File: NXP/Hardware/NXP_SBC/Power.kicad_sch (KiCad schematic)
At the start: 101 parts, among them J6 USB_C_Receptacle_PowerOnly_6P, J7 Screw_Terminal_01x02, Q1 DMN3150L-7, Q2 DMN3150L-7, Q3 DMN3150L-7, Q4 DMN3150L-7, Q5 DMN3150L-7, Q6 DMN3150L-7, Q8 DMN3150L-7, U11 AP3401, U3 AP3401, U4 AP3401, U5 MP2144GJ-P, U6 MAX811REUS-T, U9 AP3401

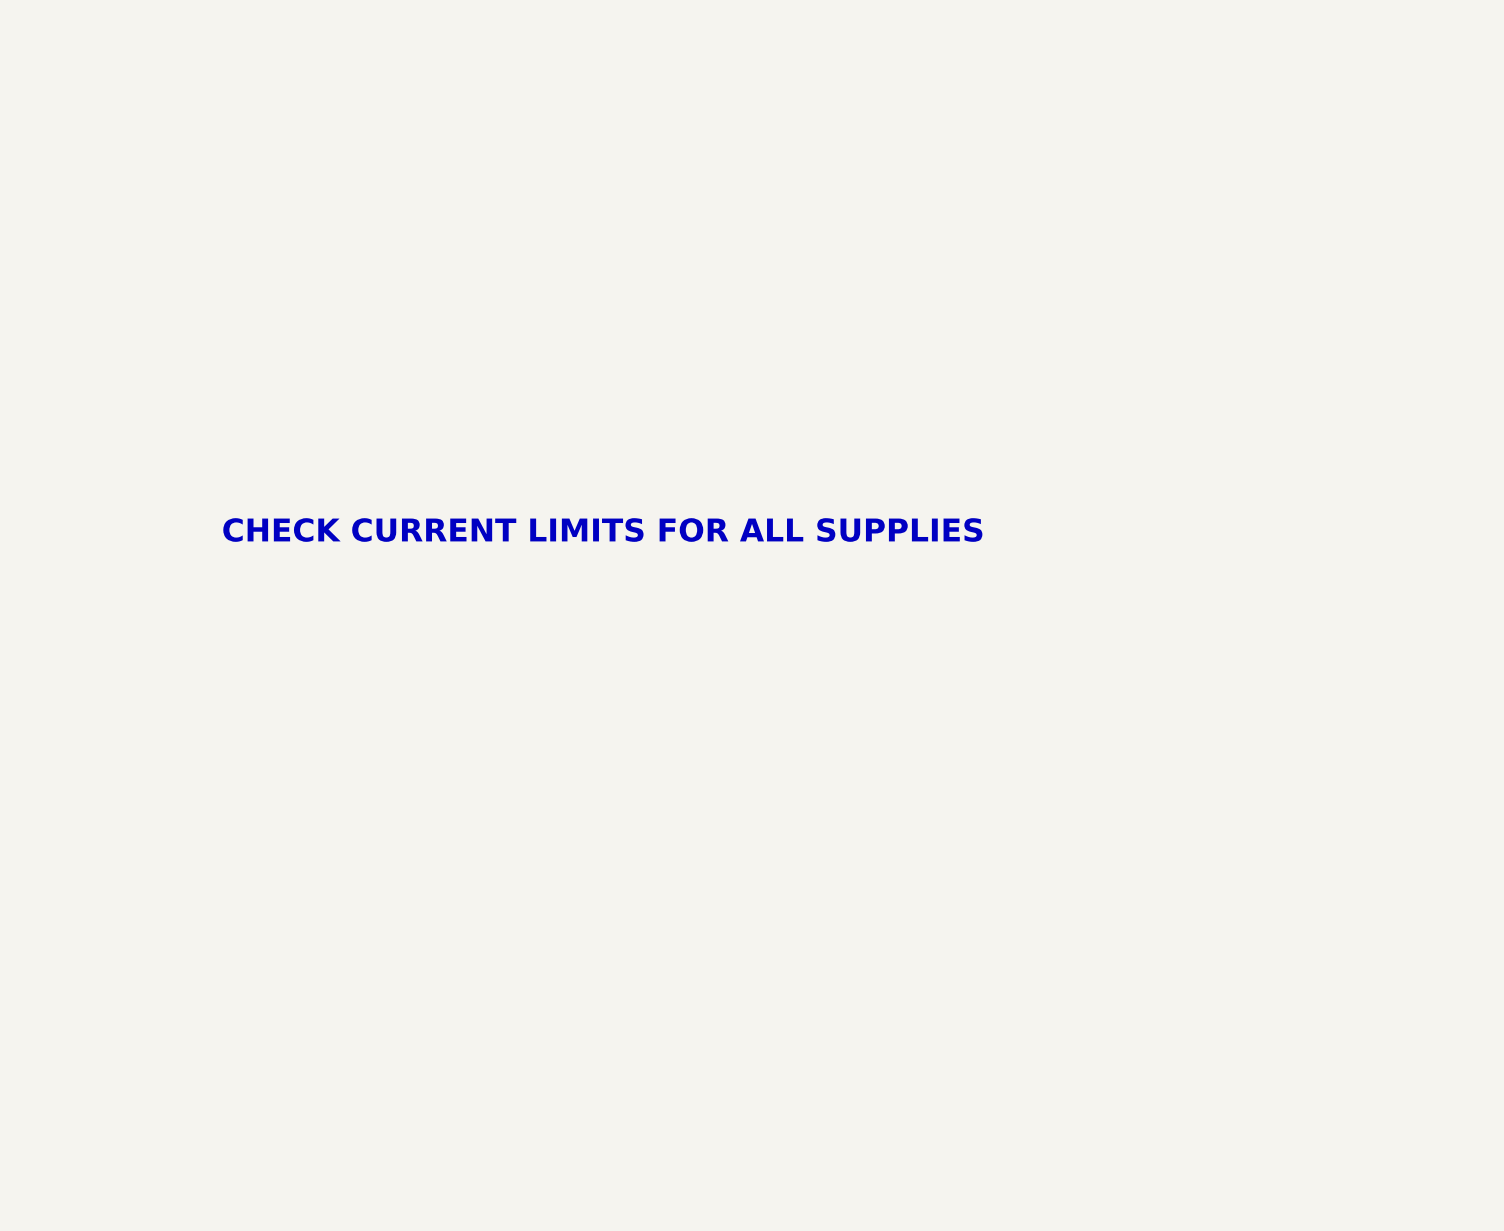
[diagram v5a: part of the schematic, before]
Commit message: Added SNVS power rail
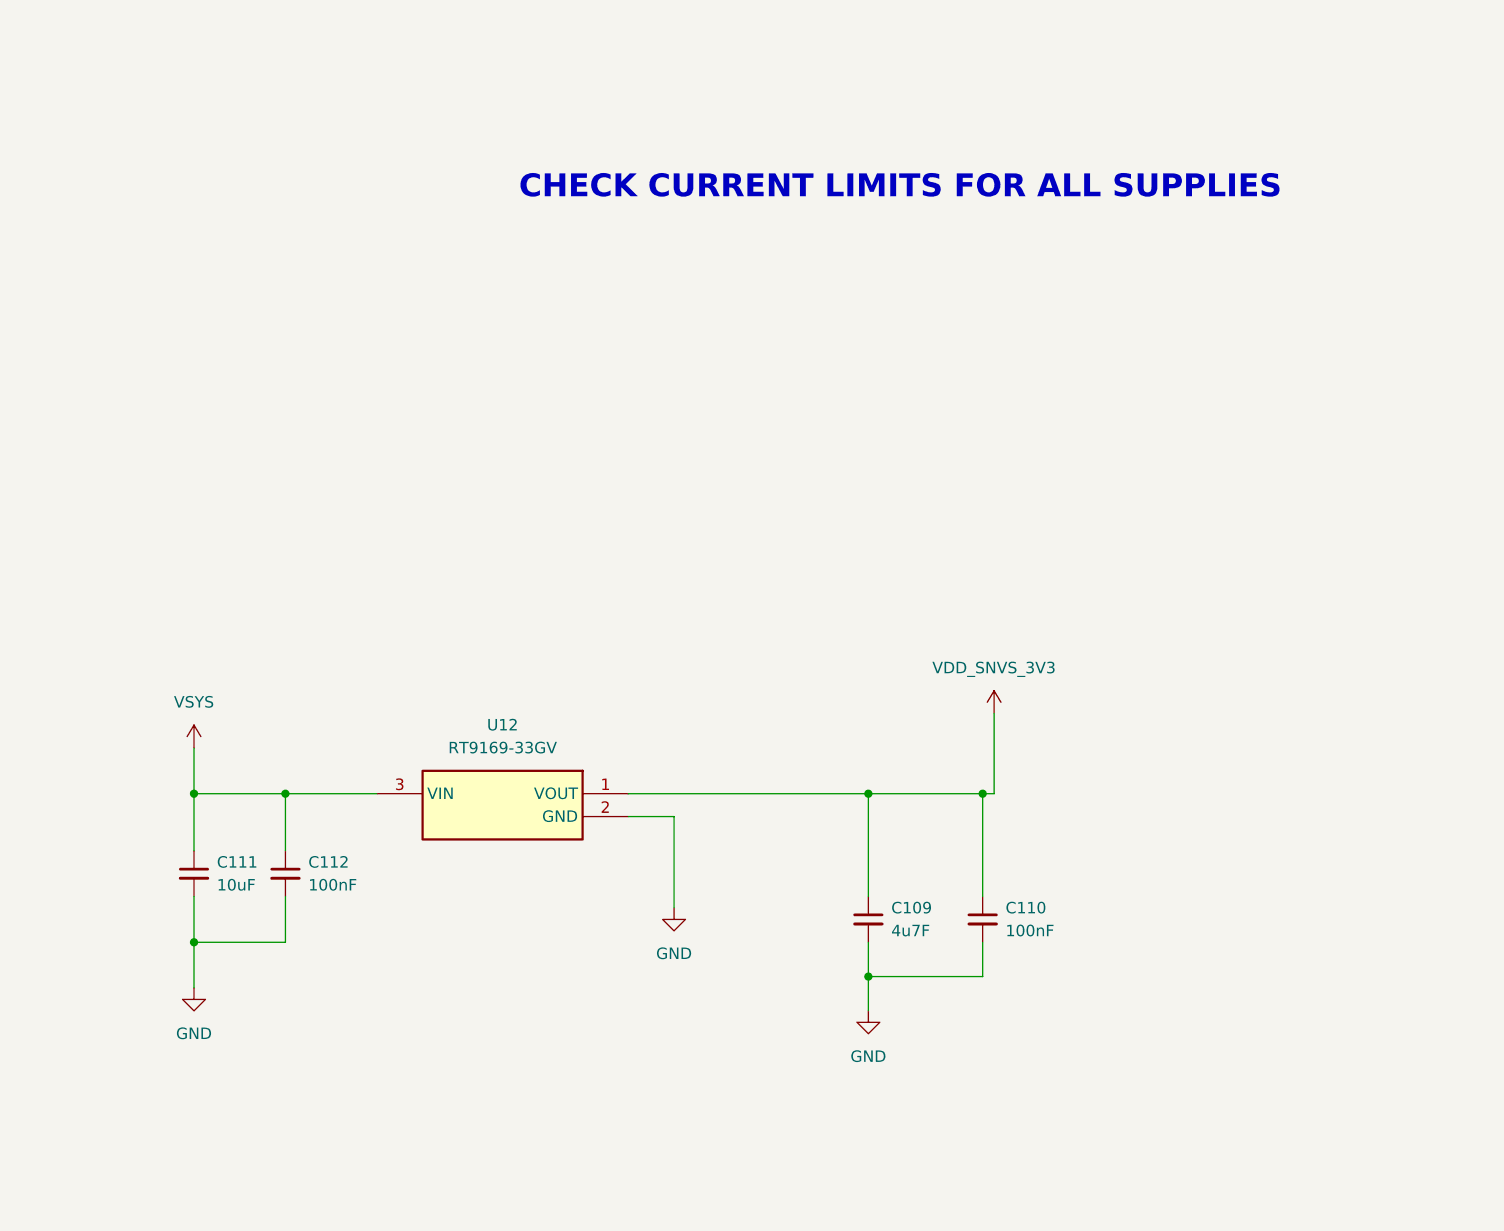
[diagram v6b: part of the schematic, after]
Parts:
- added C109: 4u7F, Capacitor_SMD:C_0603_1608Metric_Pad1.08x0.95mm_HandSolder, symbol Device:C_Small
- added C110, C112: 100nF, Capacitor_SMD:C_0603_1608Metric_Pad1.08x0.95mm_HandSolder, symbol Device:C_Small
- added C111: 10uF, Capacitor_SMD:C_0603_1608Metric_Pad1.08x0.95mm_HandSolder, symbol Device:C_Small
- added U12: RT9169-33GV, NXP_SBC:SOT95P279X130-3N, symbol NXP_SBC:RT9169-33GV
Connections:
- net GND: now also C109.2, C110.2, C111.2, C112.2, U12.2 (GND)
- net VDD_SNVS_3V3: now also C109.1, C110.1, U12.1 (VOUT)
- net VSYS: now also C111.1, C112.1, U12.3 (VIN)
